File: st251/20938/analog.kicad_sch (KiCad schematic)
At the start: 202 parts, among them J1 control, J2 data, J3 POWER, J4 SPINDLE, J5 STEPPER, J6 HEADS, J7 CONFIG, Q1 BC859, Q2 2SD1760, Q3 IRFD110, Q4 IRFD110, Q5 IRFD110

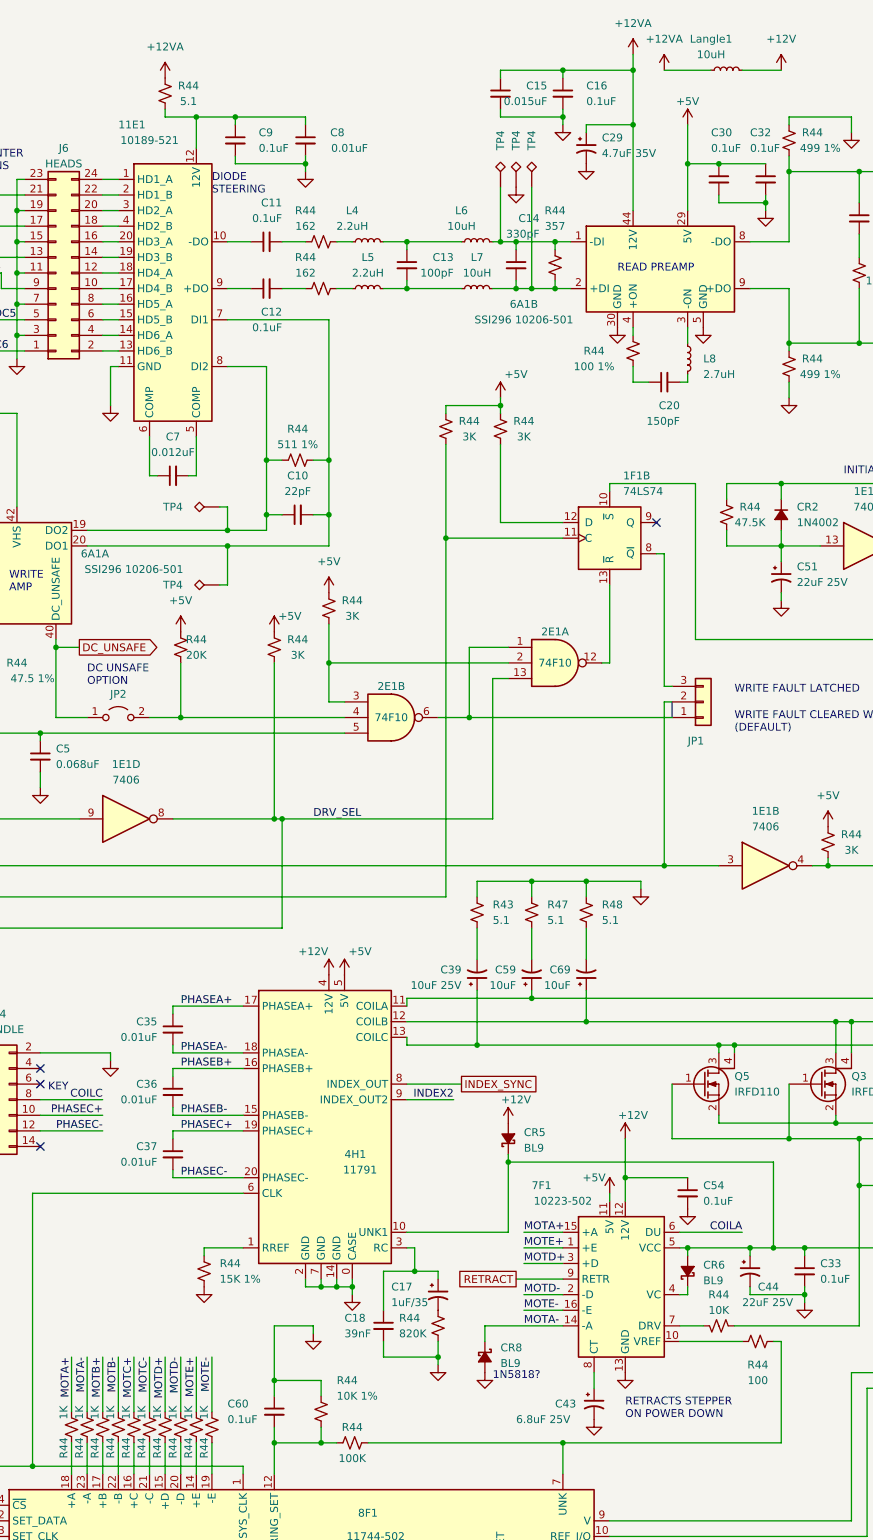
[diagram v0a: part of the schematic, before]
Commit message: Added description for RETURN ASIC
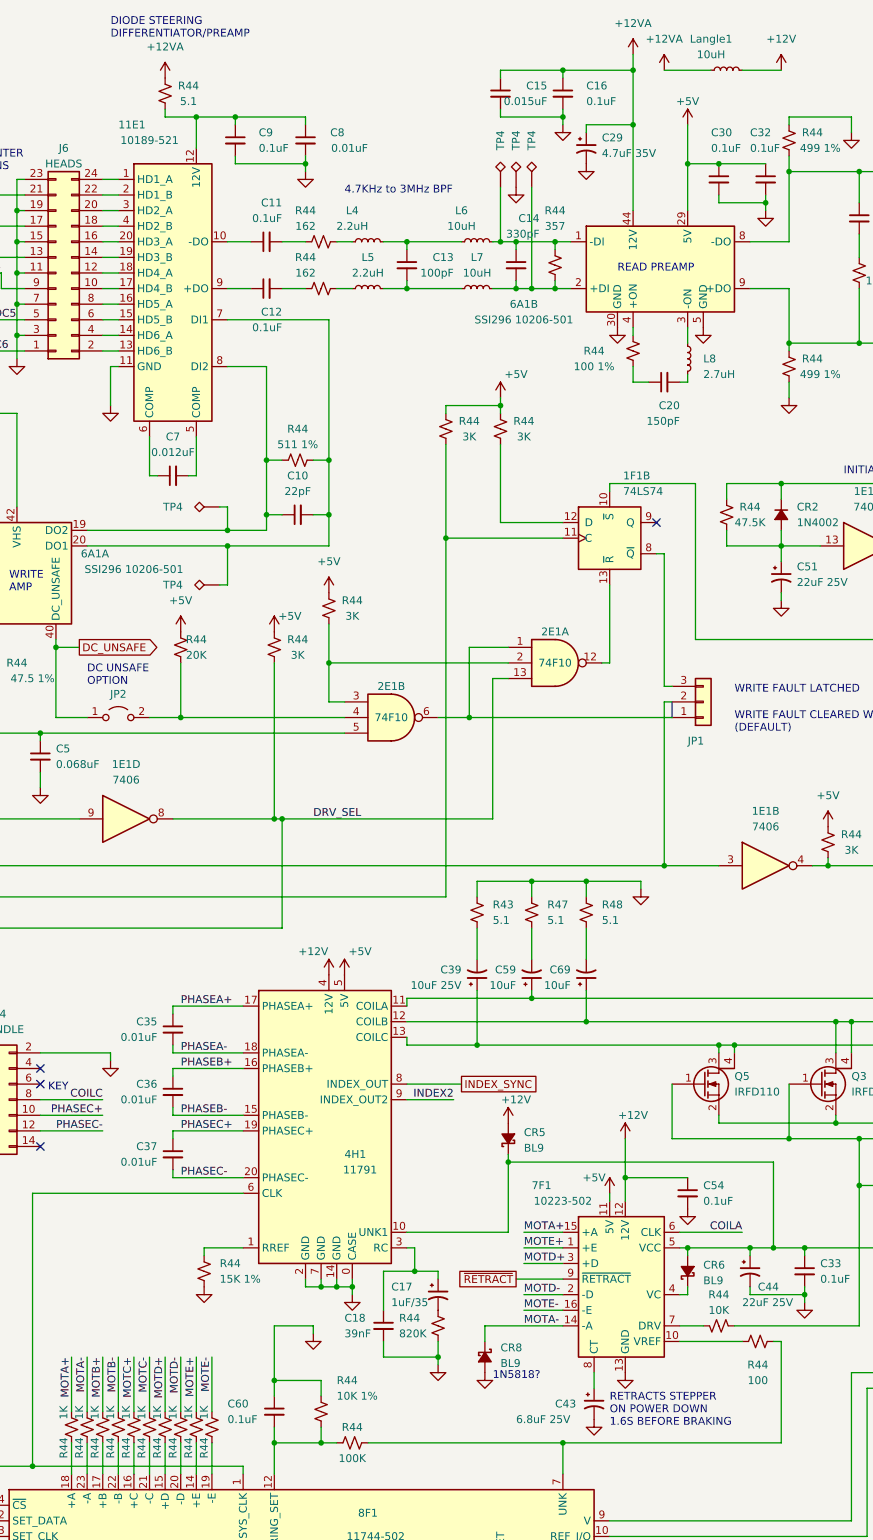
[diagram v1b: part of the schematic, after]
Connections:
- net RETRACT renamed ~{RETRACT}
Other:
- note added: "4.7KHz to 3MHz BPF"
- note added: "DIODE STEERING DIFFERENTIATOR/PREAMP"
- note added: "RETRACTS STEPPER ON POWER DOWN 1.6S BEFORE BRAKING"
- note removed: "DIODE STEERING"
- note removed: "RETRACTS STEPPER ON POWER DOWN"
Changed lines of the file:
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@@
+    (effects (font (size 1.27 1.27)) (justify left bottom))
+  )
+  (text "4.7KHz to 3MHz BPF" (at 210.82 41.91 0)
     (effects (font (size 1.27 1.27)) (justify left bottom))
   )
@@
     (effects (font (size 1.27 1.27)) (justify left bottom))
   )
-  (text "RETRACTS STEPPER\nON POWER DOWN" (at 256.54 241.3 0)
+  (text "RETRACTS STEPPER\nON POWER DOWN\n1.6S BEFORE BRAKING"
+    (at 254 242.57 0)
     (effects (font (size 1.27 1.27)) (justify left bottom))
   )
@@
     (effects (font (size 1.27 1.27)) (justify left bottom))
   )
-  (text "DIODE\nSTEERING" (at 189.23 41.91 0)
+  (text "DIODE STEERING\nDIFFERENTIATOR/PREAMP" (at 172.72 16.51 0)
     (effects (font (size 1.27 1.27)) (justify left bottom))
   )
@@
     )
   )
-  (global_label "RETRACT" (shape passive) (at 238.76 218.44 180) (fields_autoplaced)
+  (global_label "~{RETRACT}" (shape passive) (at 238.76 218.44 180) (fields_autoplaced)
     (effects (font (size 1.27 1.27)) (justify right))
     (property "Intersheetrefs" "${INTERSHEET_REFS}" (at 228.9033 218.44 0)

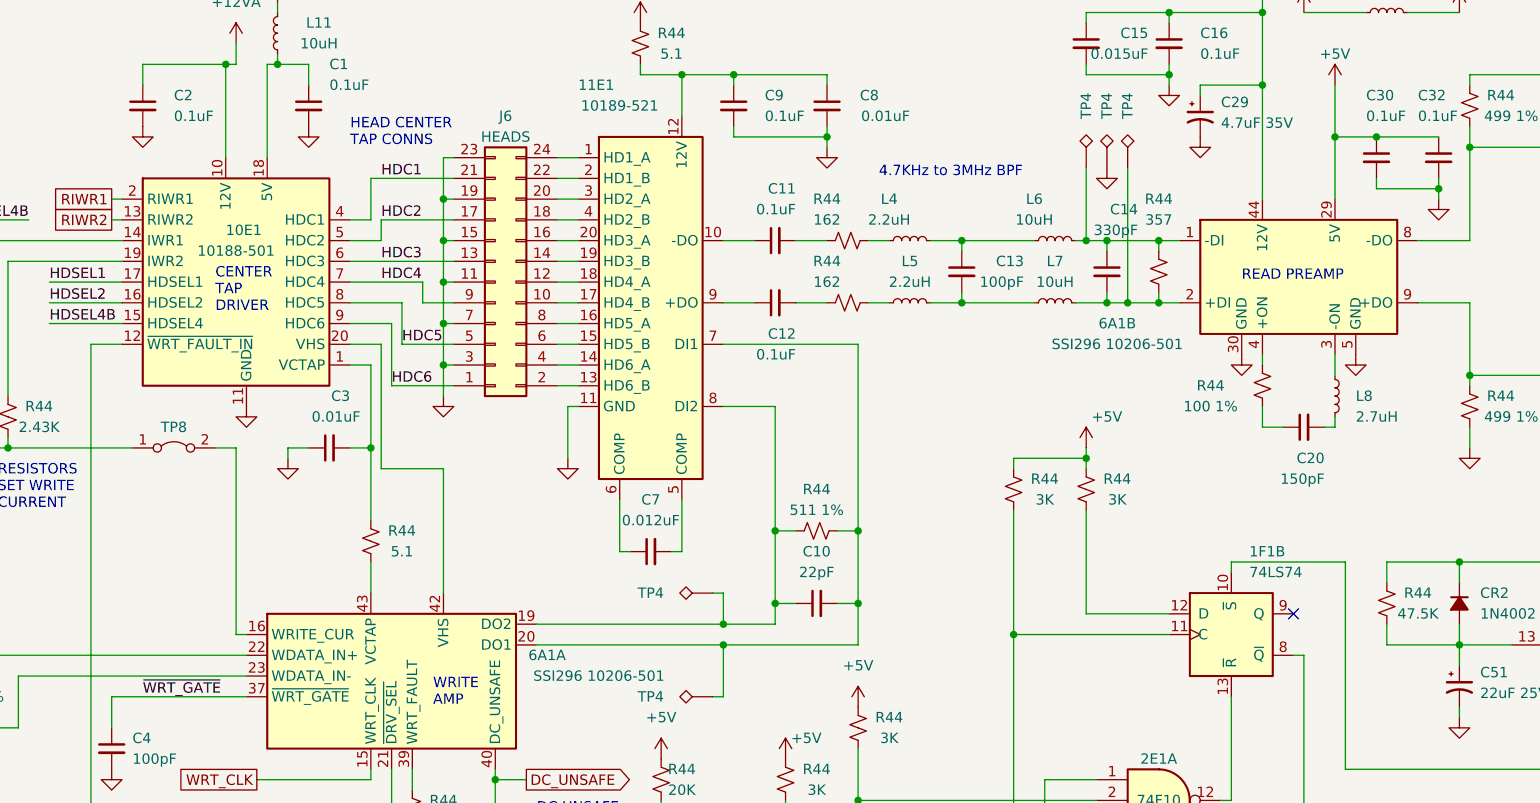
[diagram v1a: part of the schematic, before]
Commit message: Document head select and preamp chips.
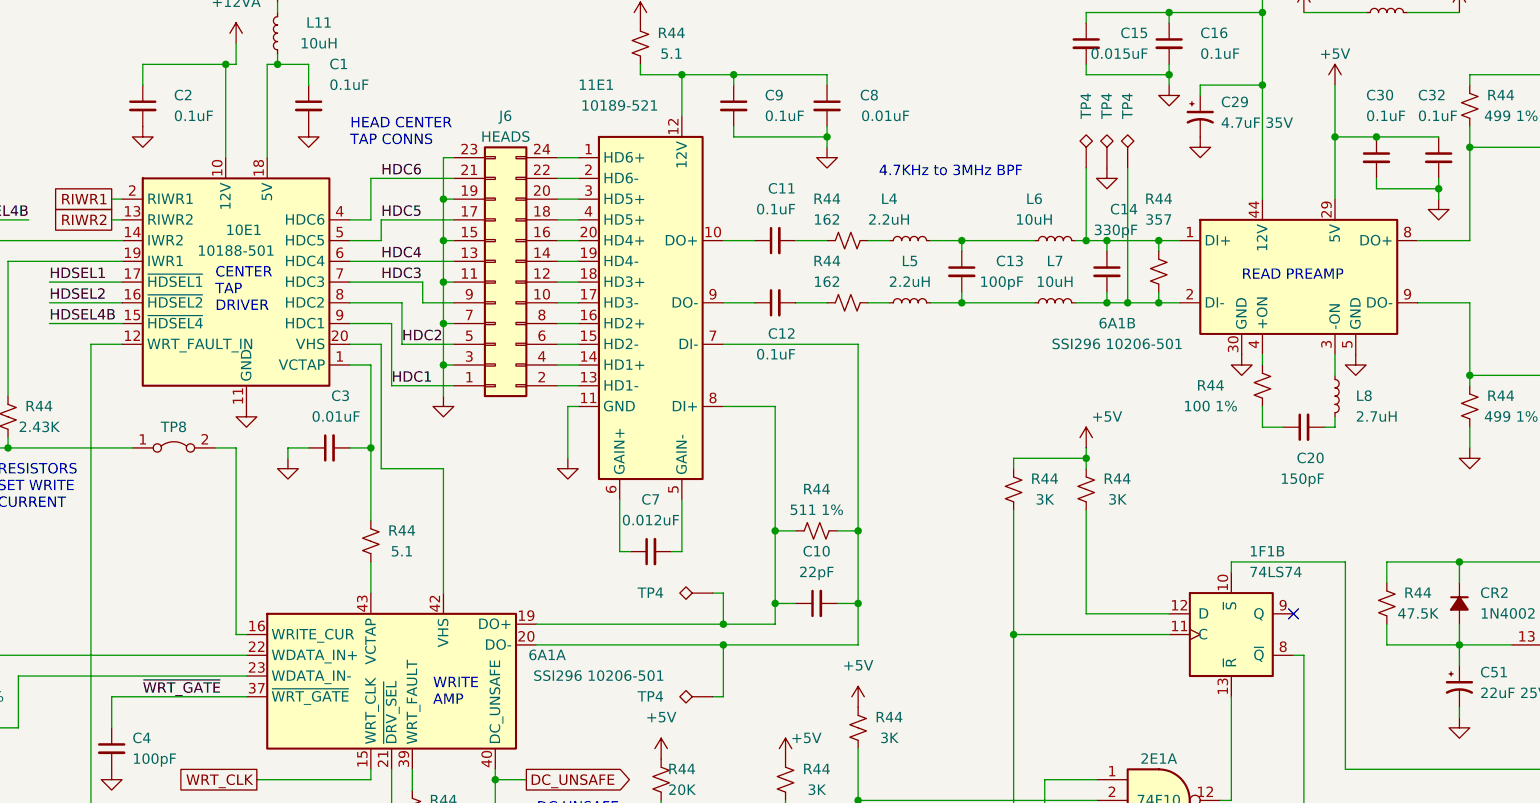
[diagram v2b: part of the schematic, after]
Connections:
- net HDC1: now also 10E1.9 (HDC1), J6.1 (Pin_1); no longer 10E1.4 (HDC1), J6.21 (Pin_21)
- net HDC2: now also 10E1.8 (HDC2), J6.5 (Pin_5); no longer 10E1.5 (HDC2), J6.17 (Pin_17)
- net HDC3: now also 10E1.7 (HDC3), J6.9 (Pin_9); no longer 10E1.6 (HDC3), J6.13 (Pin_13)
- net HDC4: now also 10E1.6 (HDC4), J6.13 (Pin_13); no longer 10E1.7 (HDC4), J6.9 (Pin_9)
- net HDC5: now also 10E1.5 (HDC5), J6.17 (Pin_17); no longer 10E1.8 (HDC5), J6.5 (Pin_5)
- net HDC6: now also 10E1.4 (HDC6), J6.21 (Pin_21); no longer 10E1.9 (HDC6), J6.1 (Pin_1)
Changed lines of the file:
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@@
     (effects (font (size 1.27 1.27)) (justify right bottom))
   )
-  (label "HDC5" (at 152.4 62.23 0) (fields_autoplaced)
+  (label "HDC5" (at 149.86 46.99 0) (fields_autoplaced)
     (effects (font (size 1.27 1.27)) (justify left bottom))
   )
@@
     (effects (font (size 1.27 1.27)) (justify left bottom))
   )
-  (label "HDC3" (at 149.86 52.07 0) (fields_autoplaced)
+  (label "HDC3" (at 149.86 54.61 0) (fields_autoplaced)
     (effects (font (size 1.27 1.27)) (justify left bottom))
   )
@@
     (effects (font (size 1.27 1.27)) (justify right bottom))
   )
-  (label "HDC1" (at 149.86 41.91 0) (fields_autoplaced)
+  (label "HDC1" (at 151.13 67.31 0) (fields_autoplaced)
     (effects (font (size 1.27 1.27)) (justify left bottom))
   )
@@
     (effects (font (size 1.27 1.27)) (justify right bottom))
   )
-  (label "HDC4" (at 149.86 54.61 0) (fields_autoplaced)
+  (label "HDC4" (at 149.86 52.07 0) (fields_autoplaced)
     (effects (font (size 1.27 1.27)) (justify left bottom))
   )
@@
     (effects (font (size 1.27 1.27)) (justify right bottom))
   )
-  (label "HDC2" (at 149.86 46.99 0) (fields_autoplaced)
+  (label "HDC2" (at 152.4 62.23 0) (fields_autoplaced)
     (effects (font (size 1.27 1.27)) (justify left bottom))
   )
@@
     (effects (font (size 1.27 1.27)) (justify right bottom))
   )
-  (label "HDC6" (at 151.13 67.31 0) (fields_autoplaced)
+  (label "HDC6" (at 149.86 41.91 0) (fields_autoplaced)
     (effects (font (size 1.27 1.27)) (justify left bottom))
   )
@@
     )
   )
-  (symbol (lib_id "st251:SSI296") (at 250.19 46.99 0) (unit 2)
+  (symbol (lib_name "SSI296_2") (lib_id "st251:SSI296") (at 250.19 46.99 0) (unit 2)
     (in_bom yes) (on_board yes) (dnp no)
     (property "Reference" "6A1" (at 240.03 59.69 0)

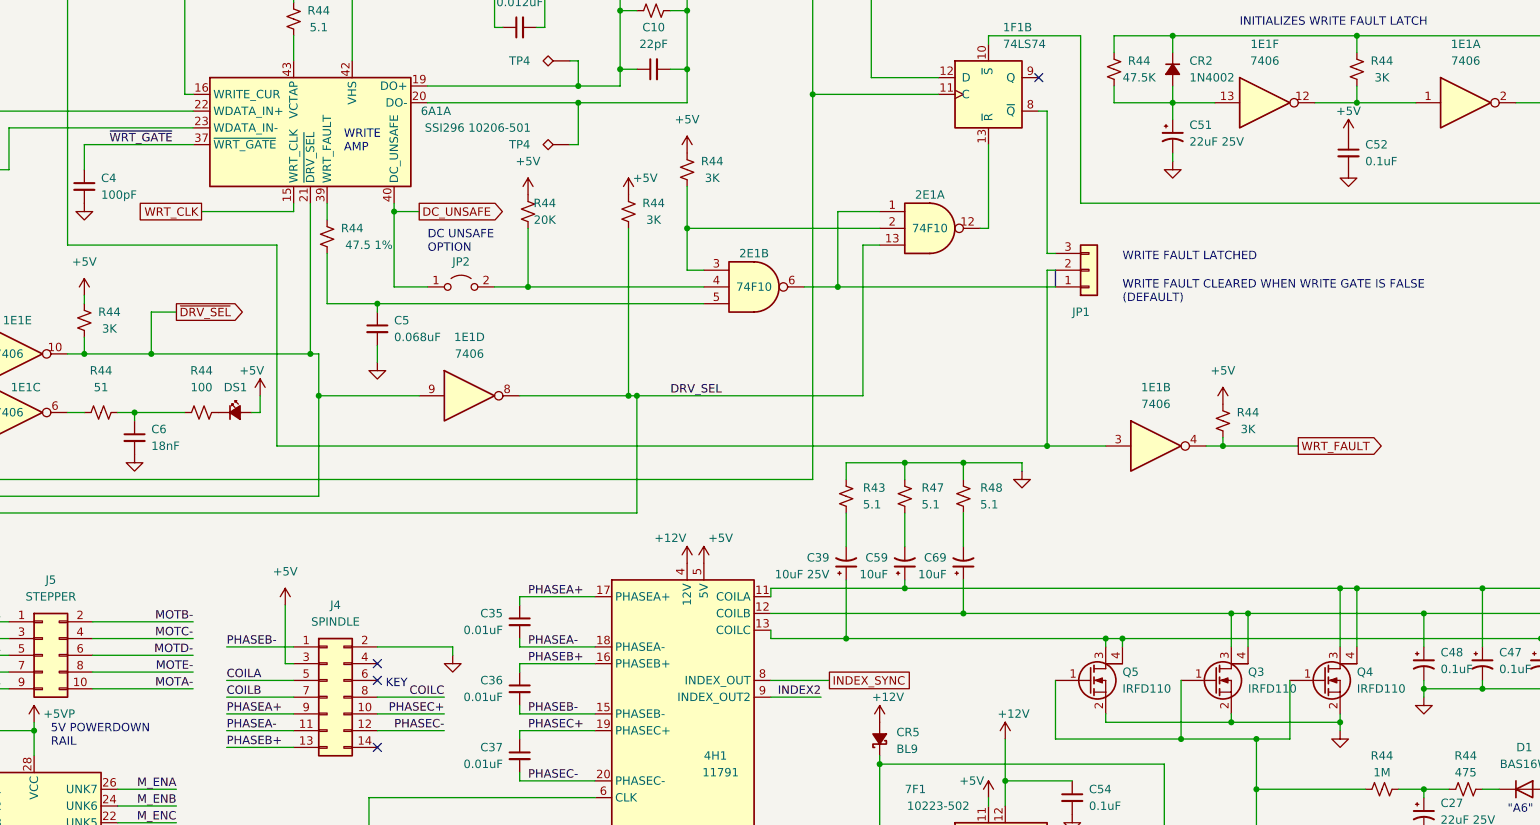
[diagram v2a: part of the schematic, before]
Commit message: Add info on MFM interface IC
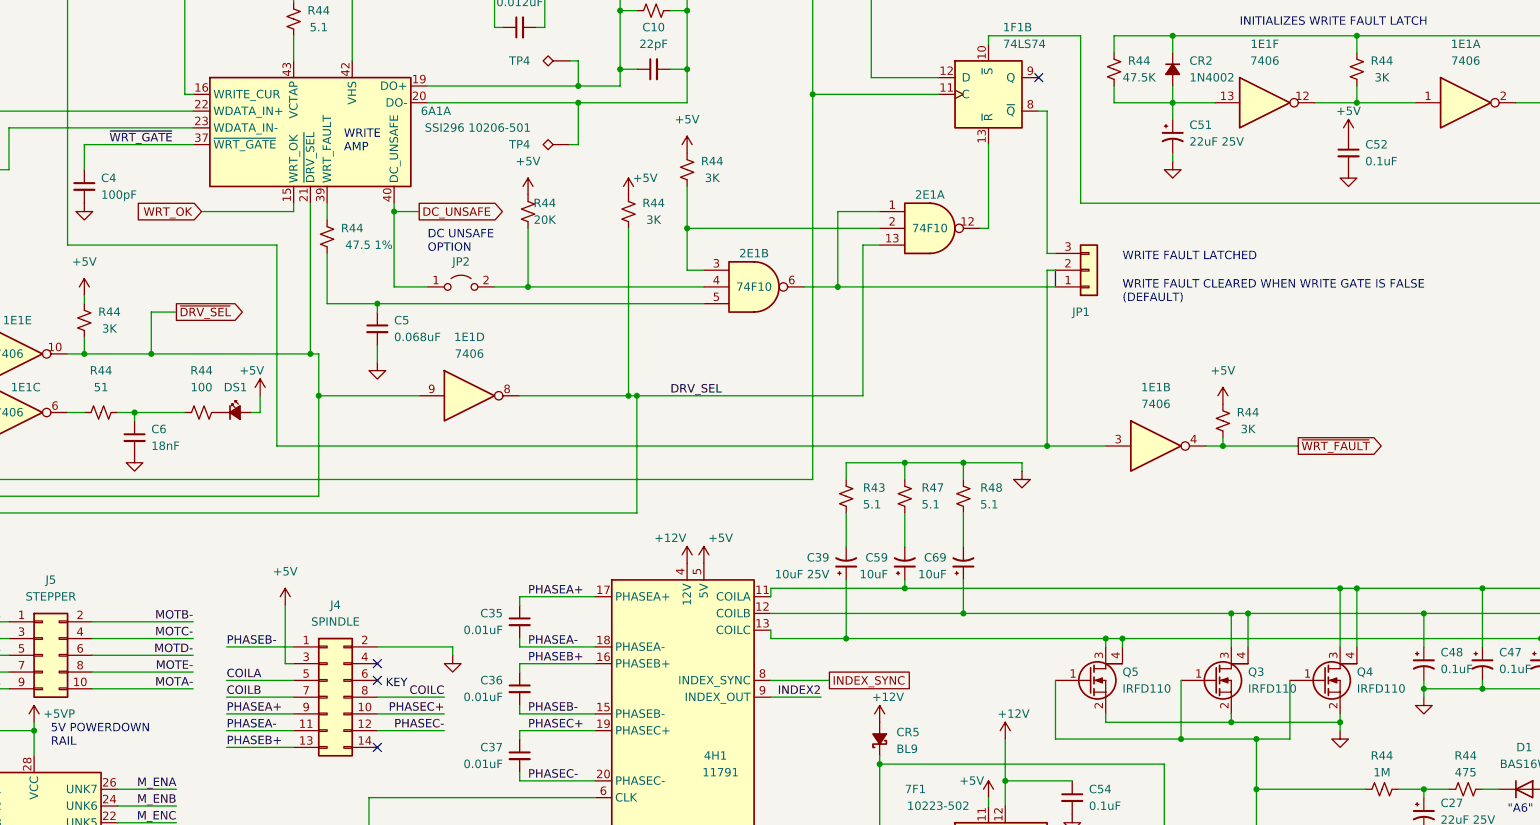
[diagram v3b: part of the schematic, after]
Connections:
- net WRT_CLK renamed WRT_OK
- net WRT_FAULT renamed ~{WRT_FAULT}
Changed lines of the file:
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@@
     )
   )
-  (global_label "WRT_FAULT" (shape output) (at 300.99 151.13 0) (fields_autoplaced)
+  (global_label "~{WRT_FAULT}" (shape output) (at 300.99 151.13 0) (fields_autoplaced)
     (effects (font (size 1.27 1.27)) (justify left))
     (property "Intersheetrefs" "${INTERSHEET_REFS}" (at 314.1352 151.13 0)
@@
     )
   )
-  (global_label "WRT_CLK" (shape passive) (at 134.62 115.57 180) (fields_autoplaced)
+  (global_label "WRT_OK" (shape input) (at 134.62 115.57 180) (fields_autoplaced)
     (effects (font (size 1.27 1.27)) (justify right))
-    (property "Intersheetrefs" "${INTERSHEET_REFS}" (at 124.5214 115.57 0)
+    (property "Intersheetrefs" "${INTERSHEET_REFS}" (at 124.3777 115.57 0)
       (effects (font (size 1.27 1.27)) (justify right) hide)
     )
